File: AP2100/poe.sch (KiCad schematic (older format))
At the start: 55 parts, among them IC1 FDS86242, Q1 HMHA2801AR2, U1 TPS23751PWP, U2 TL431DBV

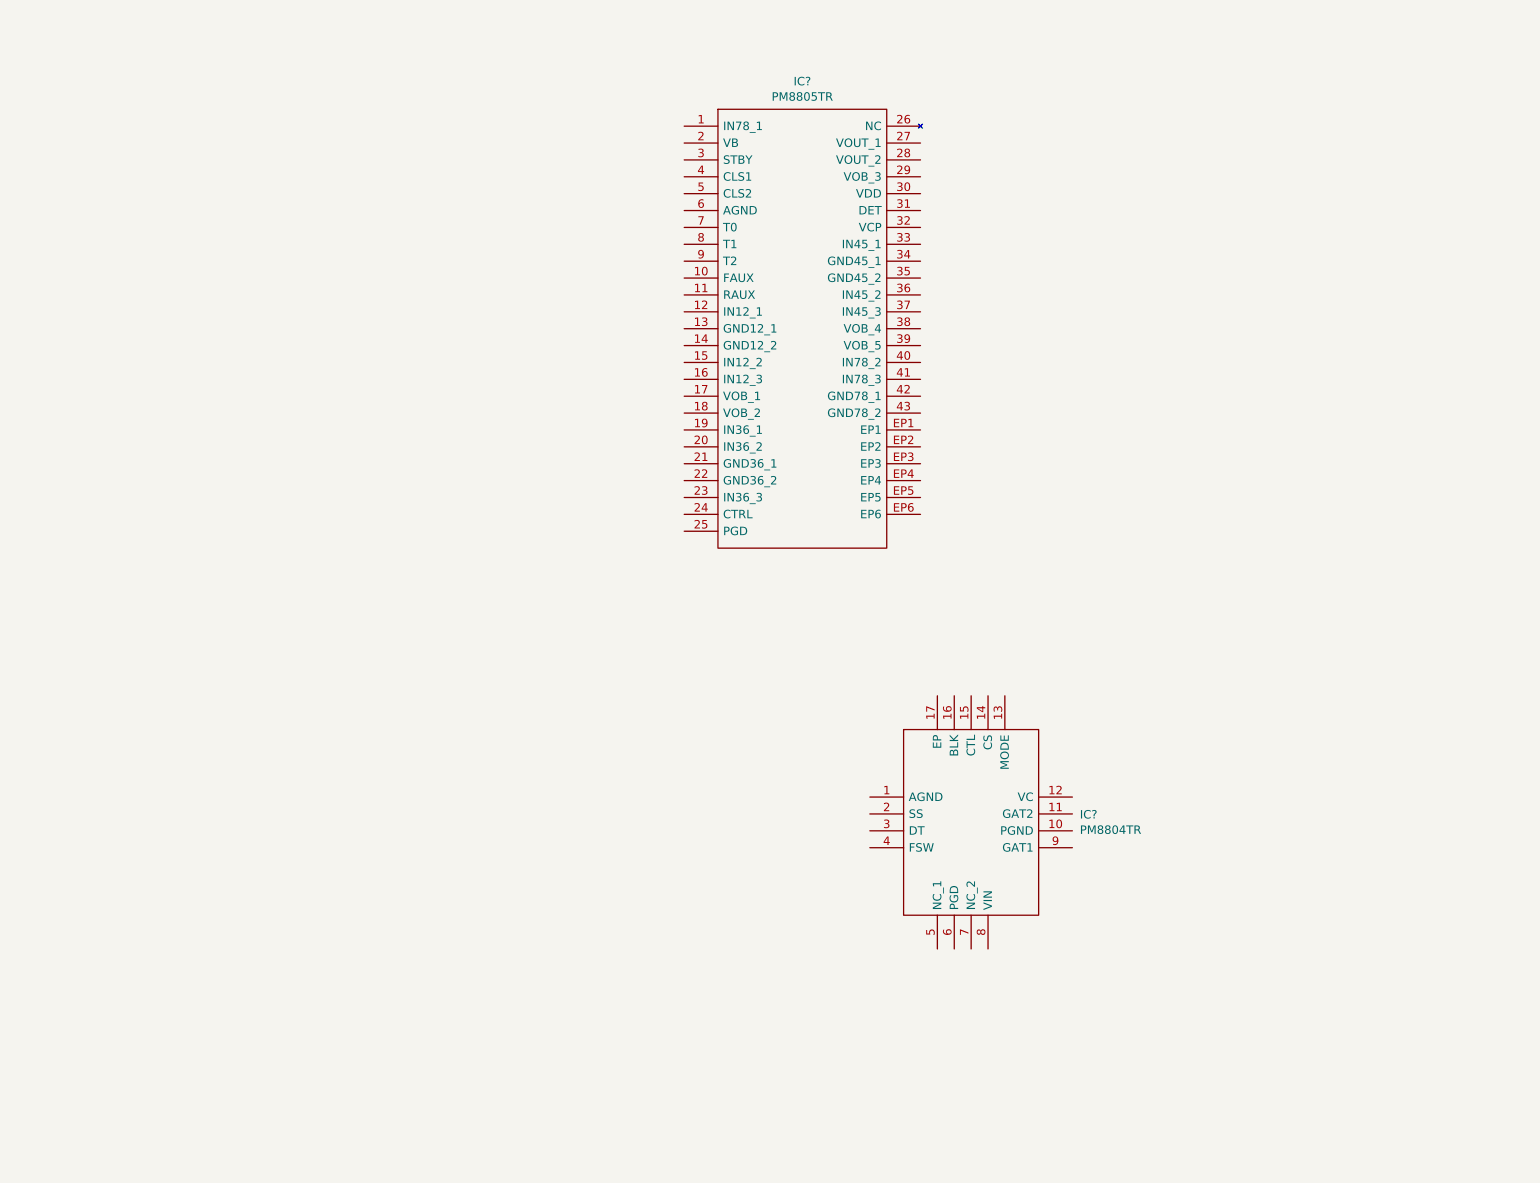
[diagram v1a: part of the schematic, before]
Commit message: Add Magjack part
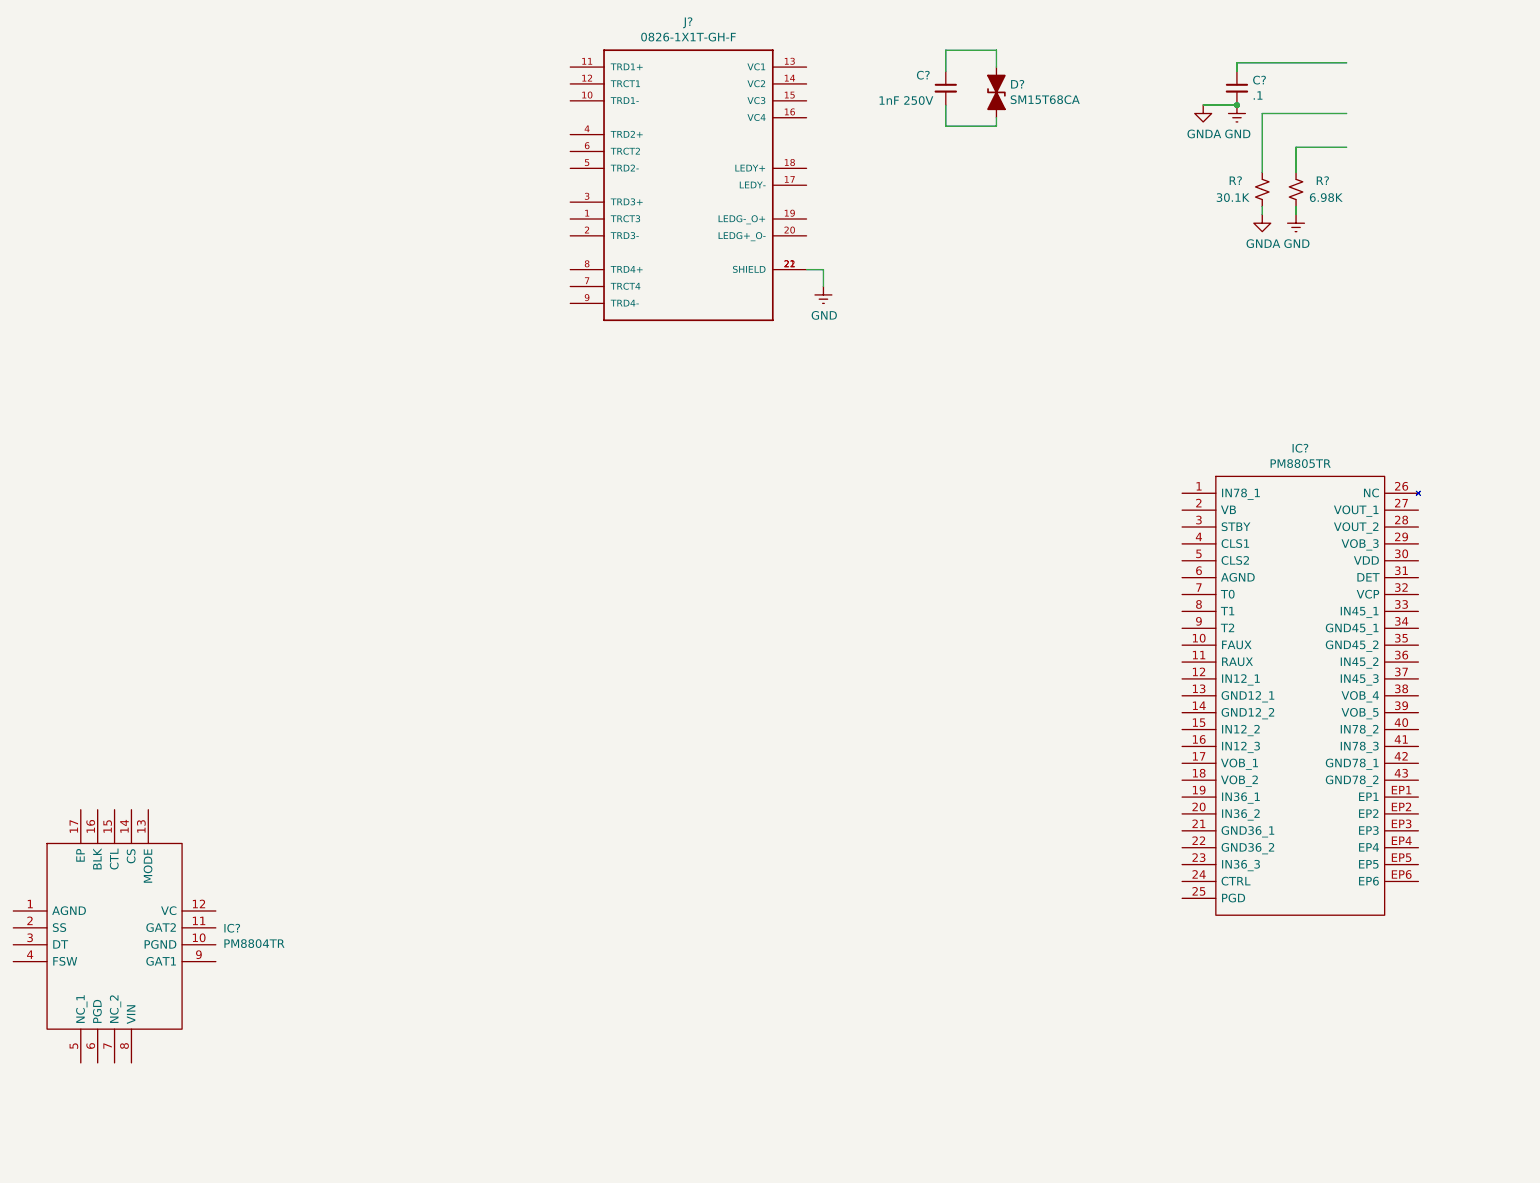
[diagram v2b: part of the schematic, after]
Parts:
- added C?: .1, Capacitor_SMD:C_0402_1005Metric, symbol Device:C_Small
- added C?: 1nF 250V, Capacitor_SMD:C_0805_2012Metric, symbol Device:C_Small
- added D?: SM15T68CA, Diode_SMD:D_SMC, symbol Device:D_TVS_ALT
- added J?: 0826-1X1T-GH-F, BEL_0826-1X1T-GH-F, symbol 0826-1X1T-GH-F:0826-1X1T-GH-F
- added R?: 30.1K, Resistor_SMD:R_0402_1005Metric, symbol Device:R_Small_US
- added R?: 6.98K, Resistor_SMD:R_0402_1005Metric, symbol Device:R_Small_US
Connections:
- net labels added: GNDA
- wire segments 221 -> 238
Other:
- moved on the sheet: IC?
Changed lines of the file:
@@
 L PM8805TR:PM8805TR IC?
 U 1 1 5EFD32AF
-P 1950 1550
-F 0 "IC?" H 2650 1815 50  0000 C CNN
-F 1 "PM8805TR" H 2650 1724 50  0000 C CNN
-F 2 "PM8805TR" H 3200 1650 50  0001 L CNN
-F 3 "https://www.st.com/resource/en/datasheet/pm8805.pdf" H 3200 1550 50  0001 L CNN
-F 4 "STMICROELECTRONICS - PM8805TR - POE/PD CONTROLLER, -40 TO 85DEG C" H 3200 1450 50  0001 L CNN "Description"
-F 5 "4" H 3200 1350 50  0001 L CNN "Height"
-F 6 "STMicroelectronics" H 3200 1250 50  0001 L CNN "Manufacturer_Name"
-F 7 "PM8805TR" H 3200 1150 50  0001 L CNN "Manufacturer_Part_Number"
-F 8 "PM8805TR" H 3200 1050 50  0001 L CNN "Arrow Part Number"
-F 9 "https://www.arrow.com/en/products/pm8805tr/stmicroelectronics" H 3200 950 50  0001 L CNN "Arrow Price/Stock"
-F 10 "511-PM8805TR" H 3200 850 50  0001 L CNN "Mouser Part Number"
-F 11 "https://www.mouser.com/Search/Refine.aspx?Keyword=511-PM8805TR" H 3200 750 50  0001 L CNN "Mouser Price/Stock"
-	1    1950 1550
+P 4900 3725
+F 0 "IC?" H 5600 3990 50  0000 C CNN
+F 1 "PM8805TR" H 5600 3899 50  0000 C CNN
+F 2 "PM8805TR" H 6150 3825 50  0001 L CNN
+F 3 "https://www.st.com/resource/en/datasheet/pm8805.pdf" H 6150 3725 50  0001 L CNN
+F 4 "STMICROELECTRONICS - PM8805TR - POE/PD CONTROLLER, -40 TO 85DEG C" H 6150 3625 50  0001 L CNN "Description"
+F 5 "4" H 6150 3525 50  0001 L CNN "Height"
+F 6 "STMicroelectronics" H 6150 3425 50  0001 L CNN "Manufacturer_Name"
+F 7 "PM8805TR" H 6150 3325 50  0001 L CNN "Manufacturer_Part_Number"
+F 8 "PM8805TR" H 6150 3225 50  0001 L CNN "Arrow Part Number"
+F 9 "https://www.arrow.com/en/products/pm8805tr/stmicroelectronics" H 6150 3125 50  0001 L CNN "Arrow Price/Stock"
+F 10 "511-PM8805TR" H 6150 3025 50  0001 L CNN "Mouser Part Number"
+F 11 "https://www.mouser.com/Search/Refine.aspx?Keyword=511-PM8805TR" H 6150 2925 50  0001 L CNN "Mouser Price/Stock"
+	1    4900 3725
 	1    0    0    -1
 $EndComp
@@
 L PM8804TR:PM8804TR IC?
 U 1 1 5EFD4BD6
-P 3050 5525
-F 0 "IC?" H 4294 5421 50  0000 L CNN
-F 1 "PM8804TR" H 4294 5330 50  0000 L CNN
-F 2 "QFN50P340X340X90-17N" H 4100 5925 50  0001 L CNN
-F 3 "https://www.st.com/resource/en/datasheet/pm8804.pdf" H 4100 5825 50  0001 L CNN
-F 4 "STMicroelectronics PM8804TR PWM Current Mode Controller, Low Side Gate Driver, 10  75V 16-Pin, VFQFPN" H 4100 5725 50  0001 L CNN "Description"
-F 5 "0.9" H 4100 5625 50  0001 L CNN "Height"
-F 6 "STMicroelectronics" H 4100 5525 50  0001 L CNN "Manufacturer_Name"
-F 7 "PM8804TR" H 4100 5425 50  0001 L CNN "Manufacturer_Part_Number"
-F 8 "PM8804TR" H 4100 5325 50  0001 L CNN "Arrow Part Number"
-F 9 "" H 4100 5225 50  0001 L CNN "Arrow Price/Stock"
-F 10 "" H 4100 5125 50  0001 L CNN "Mouser Part Number"
-F 11 "" H 4100 5025 50  0001 L CNN "Mouser Price/Stock"
-	1    3050 5525
-	1    0    0    -1
-$EndComp
+P -2025 6200
+F 0 "IC?" H -781 6096 50  0000 L CNN
+F 1 "PM8804TR" H -781 6005 50  0000 L CNN
+F 2 "QFN50P340X340X90-17N" H -975 6600 50  0001 L CNN
+F 3 "https://www.st.com/resource/en/datasheet/pm8804.pdf" H -975 6500 50  0001 L CNN
+F 4 "STMicroelectronics PM8804TR PWM Current Mode Controller, Low Side Gate Driver, 10  75V 16-Pin, VFQFPN" H -975 6400 50  0001 L CNN "Description"
+F 5 "0.9" H -975 6300 50  0001 L CNN "Height"
+F 6 "STMicroelectronics" H -975 6200 50  0001 L CNN "Manufacturer_Name"
+F 7 "PM8804TR" H -975 6100 50  0001 L CNN "Manufacturer_Part_Number"
+F 8 "PM8804TR" H -975 6000 50  0001 L CNN "Arrow Part Number"
+F 9 "" H -975 5900 50  0001 L CNN "Arrow Price/Stock"
+F 10 "" H -975 5800 50  0001 L CNN "Mouser Part Number"
+F 11 "" H -975 5700 50  0001 L CNN "Mouser Price/Stock"
+	1    -2025 6200
+	1    0    0    -1
+$EndComp
+$Comp
+L 0826-1X1T-GH-F:0826-1X1T-GH-F J?
+U 1 1 5EF63CAA
+P 1975 1900
+F 0 "J?" H 1975 2867 50  0000 C CNN
+F 1 "0826-1X1T-GH-F" H 1975 2776 50  0000 C CNN
+F 2 "BEL_0826-1X1T-GH-F" H 1975 1900 50  0001 L BNN
+F 3 "Bel Component" H 1975 1900 50  0001 L BNN
+	1    1975 1900
+	1    0    0    -1
+$EndComp
+Wire Wire Line
+	2675 2400 2775 2400
+Wire Wire Line
+	2775 2400 2775 2500
+$Comp
+L Scott:GND #PWR?
+U 1 1 5EF81E19
+P 2775 2500
+AR Path="/5EE8EF4C/5EF81E19" Ref="#PWR?"  Part="1"
+AR Path="/5ED53141/5EF81E19" Ref="#PWR?"  Part="1"
+F 0 "#PWR?" H 2775 2250 50  0001 C CNN
+F 1 "GND" H 2780 2327 50  0000 C CNN
+F 2 "" H 2775 2500 50  0001 C CNN
+F 3 "" H 2775 2500 50  0001 C CNN
+	1    2775 2500
+	1    0    0    -1
+$EndComp
+$Comp
+L Device:C_Small C?
+U 1 1 5EFB3570
+P 5225 1325
+AR Path="/5EE8EF4C/5EFB3570" Ref="C?"  Part="1"
+AR Path="/5ED53141/5EFB3570" Ref="C?"  Part="1"
+F 0 "C?" H 5317 1371 50  0000 L CNN
+F 1 ".1" H 5317 1280 50  0000 L CNN
+F 2 "Capacitor_SMD:C_0402_1005Metric" H 5225 1325 50  0001 C CNN
+F 3 "~" H 5225 1325 50  0001 C CNN
+F 4 "-" H 4175 -1025 50  0001 C CNN "MFR"
+F 5 "-" H 4175 -1025 50  0001 C CNN "MPN"
+F 6 "-" H 4175 -1025 50  0001 C CNN "SPR"
+F 7 "-" H 4175 -1025 50  0001 C CNN "SPN"
+F 8 "-" H 4175 -1025 50  0001 C CNN "SPURL"
+	1    5225 1325
+	1    0    0    -1
+$EndComp
+$Comp
+L power:GNDA #PWR?
+U 1 1 5EFB3576
+P 5025 1425
+F 0 "#PWR?" H 5025 1175 50  0001 C CNN
+F 1 "GNDA" H 5030 1252 50  0000 C CNN
+F 2 "" H 5025 1425 50  0001 C CNN
+F 3 "" H 5025 1425 50  0001 C CNN
+	1    5025 1425
+	1    0    0    -1
+$EndComp
+$Comp
+L Device:R_Small_US R?
+U 1 1 5EFB3581
+P 5375 1925
+F 0 "R?" H 5175 1975 50  0000 L CNN
+F 1 "30.1K" H 5100 1875 50  0000 L CNN
+F 2 "Resistor_SMD:R_0402_1005Metric" H 5375 1925 50  0001 C CNN
+F 3 "~" H 5375 1925 50  0001 C CNN
+F 4 "-" H 4175 -1025 50  0001 C CNN "MFR"
+F 5 "-" H 4175 -1025 50  0001 C CNN "MPN"
+F 6 "-" H 4175 -1025 50  0001 C CNN "SPR"
+F 7 "-" H 4175 -1025 50  0001 C CNN "SPN"
+F 8 "-" H 4175 -1025 50  0001 C CNN "SPURL"
+	1    5375 1925
+	1    0    0    -1
+$EndComp
+$Comp
+L Device:R_Small_US R?
+U 1 1 5EFB358C
+P 5575 1925
+F 0 "R?" H 5375 1875 50  0000 L CNN
+F 1 "6.98K" H 5300 1975 50  0000 L CNN
+F 2 "Resistor_SMD:R_0402_1005Metric" H 5575 1925 50  0001 C CNN
+F 3 "~" H 5575 1925 50  0001 C CNN
+F 4 "-" H 4175 -1025 50  0001 C CNN "MFR"
+F 5 "-" H 4175 -1025 50  0001 C CNN "MPN"
+F 6 "-" H 4175 -1025 50  0001 C CNN "SPR"
+F 7 "-" H 4175 -1025 50  0001 C CNN "SPN"
+F 8 "-" H 4175 -1025 50  0001 C CNN "SPURL"
+	1    5575 1925
+	-1   0    0    1
+$EndComp
+$Comp
+L power:GNDA #PWR?
+U 1 1 5EFB3592
+P 5375 2075
+F 0 "#PWR?" H 5375 1825 50  0001 C CNN
+F 1 "GNDA" H 5380 1902 50  0000 C CNN
+F 2 "" H 5375 2075 50  0001 C CNN
+F 3 "" H 5375 2075 50  0001 C CNN
+	1    5375 2075
+	1    0    0    -1
+$EndComp
+$Comp
+L Scott:GND #PWR?
+U 1 1 5EFB3598
+P 5225 1425
+F 0 "#PWR?" H 5225 1175 50  0001 C CNN
+F 1 "GND" H 5230 1252 50  0000 C CNN
+F 2 "" H 5225 1425 50  0001 C CNN
+F 3 "" H 5225 1425 50  0001 C CNN
+	1    5225 1425
+	1    0    0    -1
+$EndComp
+$Comp
+L Scott:GND #PWR?
+U 1 1 5EFB359E
+P 5575 2075
+F 0 "#PWR?" H 5575 1825 50  0001 C CNN
+F 1 "GND" H 5580 1902 50  0000 C CNN
+F 2 "" H 5575 2075 50  0001 C CNN
+F 3 "" H 5575 2075 50  0001 C CNN
+	1    5575 2075
+	1    0    0    -1
+$EndComp
+Wire Wire Line
+	5025 1425 5225 1425
+Wire Wire Line
+	5225 1175 5225 1225
+Wire Wire Line
+	5225 1175 5875 1175
+Wire Wire Line
+	5375 1475 5375 1825
+Wire Wire Line
+	5375 1475 5875 1475
+Wire Wire Line
+	5575 1825 5575 1675
+Wire Wire Line
+	5575 1675 5875 1675
+Wire Wire Line
+	5375 2025 5375 2075
+Wire Wire Line
+	5575 2025 5575 2075
+Connection ~ 5225 1425
+$Comp
+L Device:C_Small C?
+U 1 1 5EFC1238
+P 3500 1325
+AR Path="/5EE8EF4C/5EFC1238" Ref="C?"  Part="1"
+AR Path="/5ED53141/5EFC1238" Ref="C?"  Part="1"
+F 0 "C?" H 3325 1400 50  0000 L CNN
+F 1 "1nF 250V" H 3100 1250 50  0000 L CNN
+F 2 "Capacitor_SMD:C_0805_2012Metric" H 3500 1325 50  0001 C CNN
+F 3 "~" H 3500 1325 50  0001 C CNN
+F 4 "-" H 2450 -1025 50  0001 C CNN "MFR"
+F 5 "-" H 2450 -1025 50  0001 C CNN "MPN"
+F 6 "-" H 2450 -1025 50  0001 C CNN "SPR"
+F 7 "-" H 2450 -1025 50  0001 C CNN "SPN"
+F 8 "-" H 2450 -1025 50  0001 C CNN "SPURL"
+	1    3500 1325
+	1    0    0    -1
+$EndComp
+$Comp
+L Device:D_TVS_ALT D?
+U 1 1 5EFC2CBC
+P 3800 1350
+F 0 "D?" V 3754 1430 50  0000 L CNN
+F 1 "SM15T68CA" V 3845 1430 50  0000 L CNN
+F 2 "Diode_SMD:D_SMC" H 3800 1350 50  0001 C CNN
+F 3 "~" H 3800 1350 50  0001 C CNN
+	1    3800 1350
+	0    1    1    0
+$EndComp
+Wire Wire Line
+	3500 1225 3500 1100
+Wire Wire Line
+	3500 1100 3800 1100
+Wire Wire Line
+	3800 1100 3800 1200
+Wire Wire Line
+	3500 1550 3800 1550
+Wire Wire Line
+	3800 1550 3800 1500
+Wire Wire Line
+	3500 1425 3500 1550
 $EndSCHEMATC

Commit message: Update poe Add cap library
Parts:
- added C48: 2.2nF 2KV, Capacitor_SMD:C_1812_4532Metric, symbol Device:C_Small
- added C?: EEEFK2A330P, CAPAE1030X1050N, symbol EEEFK2A330P:EEEFK2A330P
- added C?: 1nF 250V, Capacitor_SMD:C_0805_2012Metric, symbol Device:C_Small
- added C? (x4): 33nF 100V, Capacitor_SMD:C_0805_2012Metric, symbol Device:C_Small
- added C? (x3): 10nF 100V, Capacitor_SMD:C_0603_1608Metric, symbol Device:C_Small
- added C?: 10nF 100V, Capacitor_SMD:C_0805_2012Metric, symbol Device:C_Small
- added C?: 1nF, Capacitor_SMD:C_0603_1608Metric, symbol Device:C_Small
- added D? (x5): SM15T68CA, Diode_SMD:D_SMC, symbol Device:D_TVS_ALT
- added D?: BAV70, Package_TO_SOT_SMD:SOT-23, symbol Diode:BAV70
- added D?: SMAJ58A, Diode_SMD:D_SMA, symbol Device:D_TVS_ALT
- added D?: T0, symbol Device:LED_ALT
- added D?: T1, symbol Device:LED_ALT
- added D?: T2, symbol Device:LED_ALT
- added D?: STPS4S200S, DIOM8059X265N, symbol STPS4S200S:STPS4S200S
- added D?: AUX, symbol Device:LED_ALT
- added FB? (x4): 220 OHM, Inductor_SMD:L_0805_2012Metric, symbol Device:L
- added J?: Barrel_Jack, symbol Connector:Barrel_Jack
- added R30, R31, R32, R33: 75, Resistor_SMD:R_0603_1608Metric, symbol Device:R_Small_US
- added R? (x2): 10K, Resistor_SMD:R_0603_1608Metric, symbol Device:R_Small_US
- added R?: 4.7K, Resistor_SMD:R_0603_1608Metric, symbol Device:R_Small_US
- added R?: 0, Resistor_SMD:R_2010_5025Metric, symbol Device:R_Small_US
- added R?: 26.1K, Resistor_SMD:R_0603_1608Metric, symbol Device:R_Small_US
- added R?: 36.5, Resistor_SMD:R_0805_2012Metric, symbol Device:R_Small_US
- added R?: 150, Resistor_SMD:R_0805_2012Metric, symbol Device:R_Small_US
- added R? (x3): 3.9K, Resistor_SMD:R_0603_1608Metric, symbol Device:R_Small_US
- added R?: 100K, Resistor_SMD:R_0603_1608Metric, symbol Device:R_Small_US
- IC2: renamed from IC?; footprint PM8805TR -> PM8805TR:PM8805TR
- IC3: renamed from IC?; footprint QFN50P340X340X90-17N -> PM8804TR:QFN50P340X340X90-17N
- J4: renamed from J?; footprint BEL_0826-1X1T-GH-F -> 0826-1X1T-GH-F:BEL_0826-1X1T-GH-F
- gave numbers to parts that had none: 5
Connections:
- net labels added: Chassis, ETH0_TD1_N, ETH0_TD1_P, ETH0_TD2_N, ETH0_TD2_P, ETH0_TD3_N, ETH0_TD3_P, ETH0_TD4_N, ETH0_TD4_P, PGD, RAUX, STBY, VDC, VOB
- wire segments 238 -> 472
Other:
- moved on the sheet: C30, C31, D7, IC2, IC3, R26, R27
